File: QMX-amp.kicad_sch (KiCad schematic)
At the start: 2 parts, among them J1 RF-IN, J2 RF-OUT

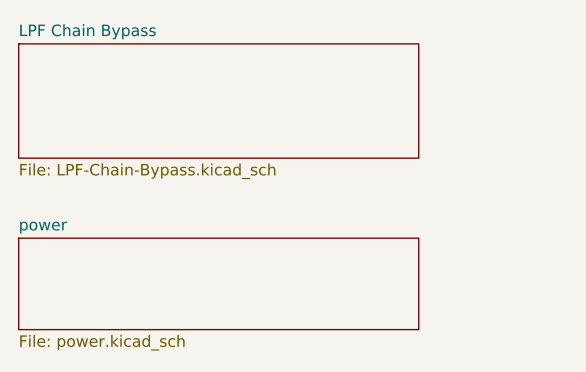
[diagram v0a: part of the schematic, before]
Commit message: all caps on LPF Chain are pF.  rest are uF
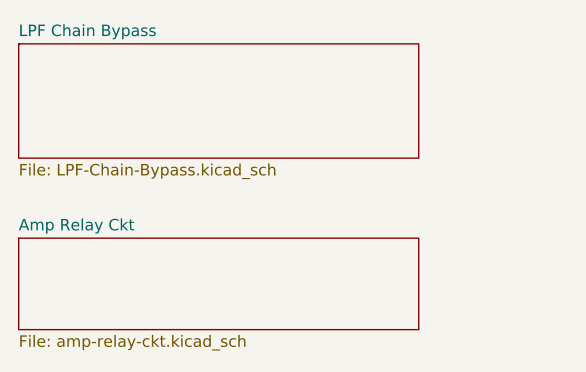
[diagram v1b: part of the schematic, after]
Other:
- sheet power renamed Amp Relay Ckt
- sheet Amp Relay Ckt: file power.kicad_sch -> amp-relay-ckt.kicad_sch
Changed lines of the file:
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@@
 	(title_block
 		(title "QMX Amp")
-		(date "2024-08-09")
-		(rev "v0.1")
+		(date "2024-08-10")
+		(rev "v0.2")
 		(company "WA7GIL")
 	)
@@
 			(color 0 0 0 0.0000)
 		)
-		(property "Sheetname" "power"
+		(property "Sheetname" "Amp Relay Ckt"
 			(at 16.51 140.2584 0)
 			(effects
@@
 			)
 		)
-		(property "Sheetfile" "power.kicad_sch"
+		(property "Sheetfile" "amp-relay-ckt.kicad_sch"
 			(at 16.51 151.7146 0)
 			(effects

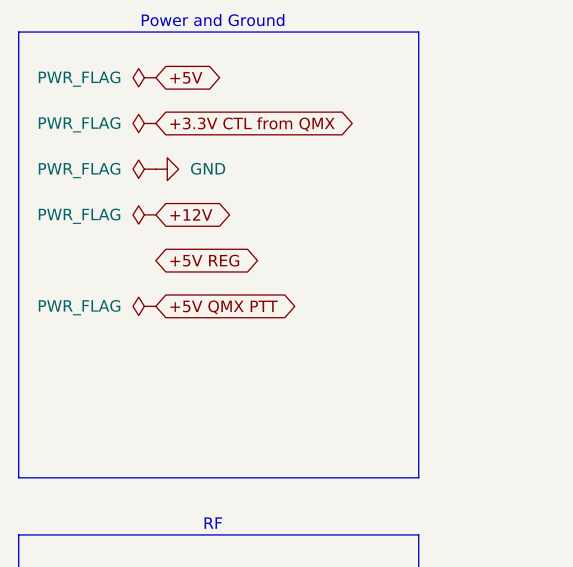
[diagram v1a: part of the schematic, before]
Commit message: +5V REG now connected to all LPF relay coils
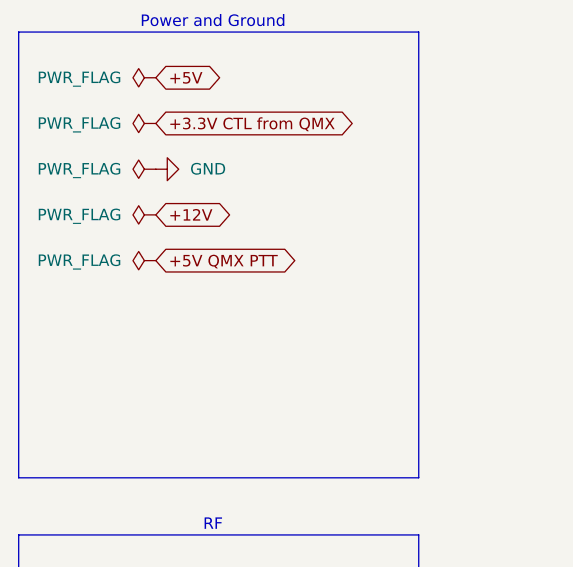
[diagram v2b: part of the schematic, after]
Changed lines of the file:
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@@
 	(global_label "+5V QMX PTT"
 		(shape bidirectional)
-		(at 31.75 53.34 0)
+		(at 31.75 48.26 0)
 		(fields_autoplaced yes)
 		(effects
@@
 		)
 		(property "Intersheetrefs" "${INTERSHEET_REFS}"
-			(at 48.8486 53.34 0)
+			(at 48.8486 48.26 0)
 			(effects
 				(font
@@
 		)
 	)
-	(global_label "+5V REG"
+	(global_label "+12V"
 		(shape bidirectional)
-		(at 31.75 48.26 0)
+		(at 31.75 43.18 0)
 		(fields_autoplaced yes)
 		(effects
@@
 		)
 		(property "Intersheetrefs" "${INTERSHEET_REFS}"
-			(at 44.3734 48.26 0)
-			(effects
-				(font
-					(size 1.27 1.27)
-				)
-				(justify left)
-				(hide yes)
-			)
-		)
-	)
-	(global_label "+12V"
+			(at 40.9263 43.18 0)
+			(effects
+				(font
+					(size 1.27 1.27)
+				)
+				(justify left)
+				(hide yes)
+			)
+		)
+	)
+	(global_label "+3.3V CTL from QMX"
 		(shape bidirectional)
-		(at 31.75 43.18 0)
+		(at 31.75 33.02 0)
 		(fields_autoplaced yes)
 		(effects
@@
 		)
 		(property "Intersheetrefs" "${INTERSHEET_REFS}"
-			(at 40.9263 43.18 0)
-			(effects
-				(font
-					(size 1.27 1.27)
-				)
-				(justify left)
-				(hide yes)
-			)
-		)
-	)
-	(global_label "+3.3V CTL from QMX"
-		(shape bidirectional)
-		(at 31.75 33.02 0)
-		(fields_autoplaced yes)
-		(effects
-			(font
-				(size 1.27 1.27)
-			)
-			(justify left)
-		)
-		(property "Intersheetrefs" "${INTERSHEET_REFS}"
 			(at 56.0452 33.02 0)
 			(effects
@@
 	(symbol
 		(lib_id "power:PWR_FLAG")
-		(at 31.75 53.34 90)
+		(at 31.75 48.26 90)
 		(unit 1)
 		(exclude_from_sim no)
@@
 		(fields_autoplaced yes)
 		(property "Reference" "#FLG05"
-			(at 29.845 53.34 0)
+			(at 29.845 48.26 0)
 			(effects
 				(font
@@
 		)
 		(property "Value" "PWR_FLAG"
-			(at 27.94 53.3399 90)
-			(effects
-				(font
-					(size 1.27 1.27)
-				)
-				(justify left)
-			)
-		)
-		(property "Footprint" ""
-			(at 31.75 53.34 0)
+			(at 27.94 48.2599 90)
+			(effects
+				(font
+					(size 1.27 1.27)
+				)
+				(justify left)
+			)
+		)
+		(property "Footprint" ""
+			(at 31.75 48.26 0)
 			(effects
 				(font
@@
 		)
 		(property "Datasheet" "~"
-			(at 31.75 53.34 0)
+			(at 31.75 48.26 0)
 			(effects
 				(font
@@
 		)
 		(property "Description" "Special symbol for telling ERC where power comes from"
-			(at 31.75 53.34 0)
-			(effects
-				(font
+			(at 31.75 48.26 0)
+			(effects
+				(font

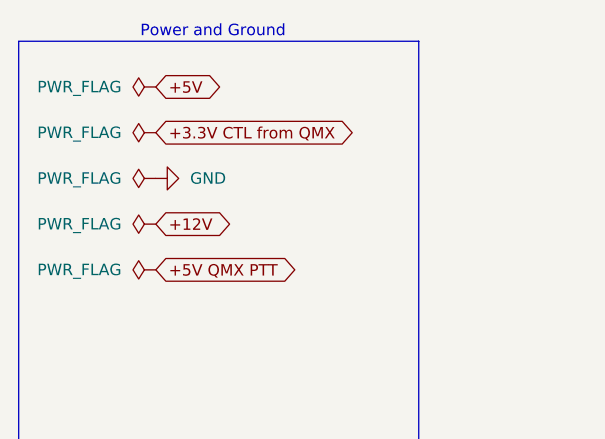
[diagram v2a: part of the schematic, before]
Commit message: changed +5V and +12V from global symbol to the more normal voltage busses
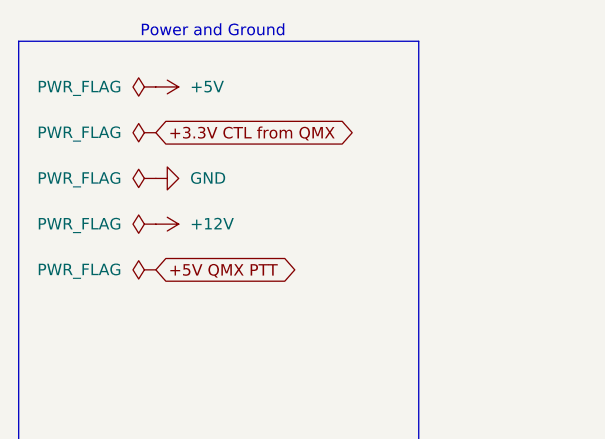
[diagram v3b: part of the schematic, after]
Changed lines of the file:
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@@
 		)
 	)
-	(global_label "+5V"
+	(global_label "+5V QMX PTT"
 		(shape bidirectional)
-		(at 31.75 27.94 0)
+		(at 31.75 48.26 0)
 		(fields_autoplaced yes)
 		(effects
@@
 		)
 		(property "Intersheetrefs" "${INTERSHEET_REFS}"
-			(at 39.7168 27.94 0)
-			(effects
-				(font
-					(size 1.27 1.27)
-				)
-				(justify left)
-				(hide yes)
-			)
-		)
-	)
-	(global_label "+5V QMX PTT"
+			(at 48.8486 48.26 0)
+			(effects
+				(font
+					(size 1.27 1.27)
+				)
+				(justify left)
+				(hide yes)
+			)
+		)
+	)
+	(global_label "RF-IN"
 		(shape bidirectional)
-		(at 31.75 48.26 0)
+		(at 43.18 93.98 0)
 		(fields_autoplaced yes)
 		(effects
@@
 		)
 		(property "Intersheetrefs" "${INTERSHEET_REFS}"
-			(at 48.8486 48.26 0)
-			(effects
-				(font
-					(size 1.27 1.27)
-				)
-				(justify left)
-				(hide yes)
-			)
-		)
-	)
-	(global_label "RF-IN"
+			(at 53.1426 93.98 0)
+			(effects
+				(font
+					(size 1.27 1.27)
+				)
+				(justify left)
+				(hide yes)
+			)
+		)
+	)
+	(global_label "+3.3V CTL from QMX"
 		(shape bidirectional)
-		(at 43.18 93.98 0)
+		(at 31.75 33.02 0)
 		(fields_autoplaced yes)
 		(effects
@@
 		)
 		(property "Intersheetrefs" "${INTERSHEET_REFS}"
-			(at 53.1426 93.98 0)
-			(effects
-				(font
-					(size 1.27 1.27)
-				)
-				(justify left)
-				(hide yes)
-			)
-		)
-	)
-	(global_label "+12V"
-		(shape bidirectional)
-		(at 31.75 43.18 0)
-		(fields_autoplaced yes)
-		(effects
-			(font
-				(size 1.27 1.27)
-			)
-			(justify left)
-		)
-		(property "Intersheetrefs" "${INTERSHEET_REFS}"
-			(at 40.9263 43.18 0)
-			(effects
-				(font
-					(size 1.27 1.27)
-				)
-				(justify left)
-				(hide yes)
-			)
-		)
-	)
-	(global_label "+3.3V CTL from QMX"
-		(shape bidirectional)
-		(at 31.75 33.02 0)
-		(fields_autoplaced yes)
-		(effects
-			(font
-				(size 1.27 1.27)
-			)
-			(justify left)
-		)
-		(property "Intersheetrefs" "${INTERSHEET_REFS}"
 			(at 56.0452 33.02 0)
 			(effects
@@
 	)
 	(symbol
+		(lib_id "power:+5V")
+		(at 31.75 27.94 270)
+		(unit 1)
+		(exclude_from_sim no)
+		(in_bom yes)
+		(on_board yes)
+		(dnp no)
+		(fields_autoplaced yes)
+		(property "Reference" "#PWR030"
+			(at 27.94 27.94 0)
+			(effects
+				(font
+					(size 1.27 1.27)
+				)
+				(hide yes)
+			)
+		)
+		(property "Value" "+5V"
+			(at 35.56 27.9399 90)
+			(effects
+				(font
+					(size 1.27 1.27)
+				)
+				(justify left)
+			)
+		)
+		(property "Footprint" ""
+			(at 31.75 27.94 0)
+			(effects
+				(font
+					(size 1.27 1.27)
+				)
+				(hide yes)
+			)
+		)
+		(property "Datasheet" ""
+			(at 31.75 27.94 0)
+			(effects
+				(font
+					(size 1.27 1.27)
+				)
+				(hide yes)
+			)
+		)
+		(property "Description" "Power symbol creates a global label with name \"+5V\""
+			(at 31.75 27.94 0)
+			(effects
+				(font
+					(size 1.27 1.27)
+				)
+				(hide yes)
+			)
+		)
+		(pin "1"
+		)
+		(instances
+			(project ""
+				(path "/e63e39d7-6ac0-4ffd-8aa3-1841a4541b55"
+					(reference "#PWR030")
+					(unit 1)
+				)
+			)
+		)
+	)
+	(symbol
 		(lib_id "power:PWR_FLAG")
 		(at 31.75 38.1 90)
@@
 					(unit 1)
 				)
+			)
+		)
+	)
+	(symbol
+		(lib_id "power:+12V")
+		(at 31.75 43.18 270)
+		(unit 1)
+		(exclude_from_sim no)
+		(in_bom yes)
+		(on_board yes)
+		(dnp no)
+		(fields_autoplaced yes)
+		(property "Reference" "#PWR03"
+			(at 27.94 43.18 0)
+			(effects
+				(font
+					(size 1.27 1.27)
+				)
+				(hide yes)
+			)
+		)
+		(property "Value" "+12V"
+			(at 35.56 43.1799 90)
+			(effects
+				(font
+					(size 1.27 1.27)
+				)
+				(justify left)
+			)
+		)
+		(property "Footprint" ""
+			(at 31.75 43.18 0)
+			(effects
+				(font
+					(size 1.27 1.27)
+				)
+				(hide yes)
+			)
+		)
+		(property "Datasheet" ""
+			(at 31.75 43.18 0)
+			(effects
+				(font
+					(size 1.27 1.27)
+				)
+				(hide yes)
+			)
+		)
+		(property "Description" "Power symbol creates a global label with name \"+12V\""
+			(at 31.75 43.18 0)
+			(effects
+				(font
+					(size 1.27 1.27)
+				)
+				(hide yes)
+			)
+		)
+		(pin "1"
+		)
+		(instances
+			(project ""
+				(path "/e63e39d7-6ac0-4ffd-8aa3-1841a4541b55"
+					(reference "#PWR03")
+					(unit 1)
+				)

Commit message: checkpoint progress from Sunday 240811
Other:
- added sheet Amp (amp.kicad_sch)
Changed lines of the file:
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@@
 		(title "QMX Amp")
 		(date "2024-08-11")
-		(rev "v0.2")
+		(rev "v0.3")
 		(company "WA7GIL")
 	)
@@
 				)
 			)
+		)
+	)
+	(sheet
+		(at 16.51 161.29)
+		(size 44.45 10.16)
+		(fields_autoplaced yes)
+		(stroke
+			(width 0.1524)
+			(type solid)
+		)
+		(fill
+			(color 0 0 0 0.0000)
+		)
+		(property "Sheetname" "Amp"
+			(at 16.51 160.5784 0)
+			(effects
+				(font
+					(size 1.27 1.27)
+				)
+				(justify left bottom)
+			)
+		)
+		(property "Sheetfile" "amp.kicad_sch"
+			(at 16.51 172.0346 0)
+			(effects
+				(font
+					(size 1.27 1.27)
+				)
+				(justify left top)
+			)
+		)
+		(instances
+			(project "QMX-amp"
+				(path "/e63e39d7-6ac0-4ffd-8aa3-1841a4541b55"
+					(page "6")
+				)
+			)
